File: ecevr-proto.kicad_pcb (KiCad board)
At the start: 4 copper layers, 100 x 92 mm, 218 parts, among them J1 Micro_SD_Card_Det, J1101 USB_microB, J1102 USB_C_Receptacle_USB2.0, J19 SFP, J2 Pwr_fallback, J20 SFP_CAGE, J2001 BNC, J2051 BNC, J2201 BEL_0845_2G1T_H5, J4 JTAG, J5 0821-1X1T-43-F, SW1 SW_Push, SW2101 SW_DIP_x08, U1 TXS0108EPW, U1101 USB3740B-AI9, U1102 UTC2000, U1103 FT231XS, U1104 74LVC1G00, U1105 SC185, U2001 74LVC2T45DC, U2051 74LVC2T45DC, U2101 74LVC1G06, U2102 74LVC1G06, U2103 PCA9306, U2104 24AA0x, U2201 74LVC1G06, U2202 74LVC1G06, U2301 lan9254, U6 PCA9546AD, U8 74AC125, U9 TPS2051B, X2301 FNETHE025

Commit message: WIP: (save)
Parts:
- removed BT1: CR1220, Battery:BatteryHolder_Keystone_500
- removed C1101, C1102, C1103, C1105, C1107: 100nF_603, Capacitor_SMD:C_0603_1608Metric
- removed C1104, C1106, C1108: 22uF_lo_ESR, Capacitor_SMD:C_1812_4532Metric
- removed D1101, D1102, D1103: LED, LED_SMD:LED_0603_1608Metric
- removed FL1101, FL1102, FL3: EMI_Filter_LL_14, proj_footprints:WE_CNSW
- removed H1, H2, H3, H4: MountingHole_Pad, MountingHole:MountingHole_3.2mm_M3_ISO14580_Pad_TopBottom
- removed J1101: USB_microB, Connector_USB:USB_Micro-B_Molex-105017-0001
- removed J1102: USB_C_Receptacle_USB2.0, proj_footprints:USB_C_Receptacle_GCT_USB4085_smaller_holes
- removed J5: 0821-1X1T-43-F, proj_footprints:BEL_0821-1X1T-43-F
- removed JB1: LSHM-150-04_JB1, Connector_Samtec:Samtec_LSHM-150-xx.x-x-DV-S_2x50-1SH_P0.50mm_Vertical
- removed JB2: LSHM-150-04_JB2, Connector_Samtec:Samtec_LSHM-150-xx.x-x-DV-S_2x50-1SH_P0.50mm_Vertical
- removed JB3: LSHM-130-04_JB3, Connector_Samtec:Samtec_LSHM-130-xx.x-x-DV-S_2x30-1SH_P0.50mm_Vertical
- removed JP1101: Jumper_3_Bridged12, Connector_PinHeader_2.54mm:PinHeader_1x03_P2.54mm_Vertical
- removed JP1102: Jumper_NO_Small, Connector_PinHeader_2.54mm:PinHeader_1x02_P2.54mm_Vertical
- removed L1101: 1uH, proj_footprints:L_TDK_SPM6530
- removed R1101, R1104, R1109, R1110: 5k1, Resistor_SMD:R_0603_1608Metric
- removed R1102, R1103, R1116, R1117: 100k, Resistor_SMD:R_0603_1608Metric
- removed R1105, R1106, R1107, R1108, R1111: 10k, Resistor_SMD:R_0603_1608Metric
- removed R1112: 35k7, Resistor_SMD:R_0603_1608Metric
- removed R1113, R1114, R1118: 1k, Resistor_SMD:R_0603_1608Metric
- removed R1115: 1, Resistor_SMD:R_0603_1608Metric
- removed RN1, RN2: 4x4k7, Resistor_SMD:R_Array_Convex_4x0603
- removed U1101: USB3740B-AI9, Package_DFN_QFN:UQFN-10_1.6x2.1mm_P0.5mm
- removed U1102: UTC2000, proj_footprints:QFN-16-1EP_3x3mm_P0.5mm_EP1.8x1.8mm
- removed U1103: FT231XS, Package_SO:SSOP-20_3.9x8.7mm_P0.635mm
- removed U1104: 74LVC1G00, Package_TO_SOT_SMD:SOT-23-5
- removed U1105: SC185, proj_footprints:QFN-16-1EP_3x3mm_P0.5mm_EP1.8x1.8mm
- added C10: 470n, Capacitor_SMD:C_0402_1005Metric, B.Cu at (56.9, 78.0)
- added C11: 100n, Capacitor_SMD:C_0402_1005Metric, B.Cu at (48.7, 72.5)
- added C16: 470n, Capacitor_SMD:C_0402_1005Metric, B.Cu at (56.9, 83.5)
- added C17: 470n, Capacitor_SMD:C_0402_1005Metric, B.Cu at (52.5, 81.7)
- added C18: 4u7, Capacitor_SMD:C_0805_2012Metric, F.Cu at (183.5, 155.2)
- added C19: 470n, Capacitor_SMD:C_0402_1005Metric, B.Cu at (53.9, 79.5)
- added C20: 470n, Capacitor_SMD:C_0402_1005Metric, B.Cu at (53.9, 81.4)
- added C21: 100u, proj_footprints:C_pol_1210_3225Metric, F.Cu at (188.8, 143.7)
- added C22: 470n, Capacitor_SMD:C_0603_1608Metric, F.Cu at (197.7, 146.2)
- added C23: 100n, Capacitor_SMD:C_0402_1005Metric, B.Cu at (45.5, 73.6)
- added C2323: 100n, Capacitor_SMD:C_0603_1608Metric, F.Cu at (172.3, 56.6)
- added C24: 100n, Capacitor_SMD:C_0402_1005Metric, B.Cu at (46.3, 75.2)
- added C25: 4u7, Capacitor_SMD:C_0805_2012Metric, F.Cu at (188.2, 150.3)
- added C26: 47u, Capacitor_SMD:C_1210_3225Metric, F.Cu at (157.8, 195.1)
- added C27: 47u, Capacitor_SMD:C_1210_3225Metric, F.Cu at (165.5, 170.3)
- added C28: 4u7, Capacitor_SMD:C_0805_2012Metric, F.Cu at (161.9, 176.9)
- added C29: 4u7, Capacitor_SMD:C_0805_2012Metric, F.Cu at (169.3, 173.9)
- added C30: 470n, Capacitor_SMD:C_0402_1005Metric, B.Cu at (59.1, 82.1)
- added C31: 470n, Capacitor_SMD:C_0402_1005Metric, B.Cu at (59.1, 85.5)
- added C32: 470n, Capacitor_SMD:C_0402_1005Metric, B.Cu at (52.3, 86.4)
- added C33: 470n, Capacitor_SMD:C_0402_1005Metric, B.Cu at (55.7, 84.9)
- added C34: 47p, Capacitor_SMD:C_0603_1608Metric, F.Cu at (196.3, 161.4)
- added C35: 47p, Capacitor_SMD:C_0603_1608Metric, F.Cu at (191.7, 167.7)
- added C36: 100n, Capacitor_SMD:C_0603_1608Metric, F.Cu at (192.3, 163.9)
- added C37: 10u, Capacitor_SMD:C_1206_3216Metric, F.Cu at (186.9, 168.1)
- added C38: 100n, Capacitor_SMD:C_0603_1608Metric, F.Cu at (196.3, 163.9)
- added C39: 100n, Capacitor_SMD:C_0603_1608Metric, F.Cu at (200.3, 161.4)
- added C40: 470n, Capacitor_SMD:C_0402_1005Metric, B.Cu at (56.2, 75.7)
- added C41: 470n, Capacitor_SMD:C_0402_1005Metric, B.Cu at (59.1, 77.5)
- added C42: 470n, Capacitor_SMD:C_0402_1005Metric, B.Cu at (59.1, 73.5)
- added C43: 470n, Capacitor_SMD:C_0402_1005Metric, B.Cu at (54.3, 75.1)
- added C44: 4u7, Capacitor_SMD:C_0805_2012Metric, F.Cu at (164.9, 173.9)
- added C45: 4u7, Capacitor_SMD:C_0805_2012Metric, F.Cu at (161.9, 179.9)
- added C46: 47u, Capacitor_SMD:C_1210_3225Metric, F.Cu at (171.1, 170.3)
- added C47: 470n, Capacitor_SMD:C_0402_1005Metric, B.Cu at (49.5, 83.1)
- added C48: 470n, Capacitor_SMD:C_0402_1005Metric, B.Cu at (49.5, 84.7)
- added C49: 470n, Capacitor_SMD:C_0402_1005Metric, B.Cu at (46.7, 84.2)
- added C50: 470n, Capacitor_SMD:C_0402_1005Metric, B.Cu at (48.9, 86.2)
- added C51: 4u7, Capacitor_SMD:C_0805_2012Metric, F.Cu at (211.4, 141.4)
- added C52: 4u7, Capacitor_SMD:C_0805_2012Metric, F.Cu at (217.0, 137.2)
- added C53: 47u, Capacitor_SMD:C_1210_3225Metric, F.Cu at (212.0, 137.8)
- added C54: 10u, Capacitor_SMD:C_1206_3216Metric, F.Cu at (25.4, 108.7)
- added C55: 10u, Capacitor_SMD:C_1206_3216Metric, F.Cu at (23.3, 74.5)
- added C6: 4u7, Capacitor_SMD:C_0805_2012Metric, F.Cu at (193.9, 143.0)
- added C62: 10u, Capacitor_SMD:C_1206_3216Metric, F.Cu at (24.3, 86.0)
- added C63: 10u, Capacitor_SMD:C_1206_3216Metric, F.Cu at (25.6, 122.9)
- added C64: 10u, Capacitor_SMD:C_1206_3216Metric, F.Cu at (155.2, 33.2)
- added C65: 22u, Capacitor_SMD:C_1206_3216Metric, F.Cu at (21.5, 100.6)
- added C66: 22u, Capacitor_SMD:C_1206_3216Metric, F.Cu at (26.4, 68.7)
- added C67: 22u, Capacitor_SMD:C_1206_3216Metric, F.Cu at (25.1, 80.3)
- added C68: 10u, Capacitor_SMD:C_1206_3216Metric, F.Cu at (25.2, 115.8)
- added C69: 10u, Capacitor_SMD:C_1206_3216Metric, F.Cu at (155.6, 40.2)
- added C7: 4u7, Capacitor_SMD:C_0805_2012Metric, F.Cu at (174.6, 155.2)
- added C70: 86p, Capacitor_SMD:C_0603_1608Metric, F.Cu at (28.4, 102.3)
- added C71: 86p, Capacitor_SMD:C_0603_1608Metric, F.Cu at (29.8, 69.5)
- added C72: 56p, Capacitor_SMD:C_0603_1608Metric, F.Cu at (28.5, 81.1)
- added C73: 56p, Capacitor_SMD:C_0603_1608Metric, F.Cu at (28.6, 116.6)
- added C74: 130p, Capacitor_SMD:C_0603_1608Metric, F.Cu at (152.2, 39.5)
- added C75: 22u, Capacitor_SMD:C_1206_3216Metric, F.Cu at (25.0, 101.6)
- added C76: 22u, Capacitor_SMD:C_1206_3216Metric, F.Cu at (24.1, 68.7)
- added C77: 100n, Capacitor_SMD:C_0603_1608Metric, F.Cu at (141.3, 160.0)
- added C78: 100n, Capacitor_SMD:C_0603_1608Metric, F.Cu at (163.6, 47.0)
- added C79: 1u, Capacitor_SMD:C_0805_2012Metric, F.Cu at (161.8, 44.4)
- added C8: 4u7, Capacitor_SMD:C_0805_2012Metric, F.Cu at (188.2, 147.3)
- added C80: 100n, Capacitor_SMD:C_0603_1608Metric, F.Cu at (158.4, 45.4)
- added C81: 100n, Capacitor_SMD:C_0603_1608Metric, F.Cu at (156.8, 50.7)
- added C82: 100n, Capacitor_SMD:C_0603_1608Metric, F.Cu at (160.4, 52.8)
- added C83: C_Small, Capacitor_SMD:C_0603_1608Metric, F.Cu at (151.6, 48.5)
- added C84: C_Small, Capacitor_SMD:C_0603_1608Metric, F.Cu at (151.6, 47.0)
- added C85: 100n, Capacitor_SMD:C_0603_1608Metric, F.Cu at (158.9, 52.8)
- added C86: 100n, Capacitor_SMD:C_0603_1608Metric, F.Cu at (156.7, 52.9)
- added C87: 100n, Capacitor_SMD:C_0603_1608Metric, F.Cu at (156.8, 47.7)
- added C88: 1u, Capacitor_SMD:C_0805_2012Metric, F.Cu at (156.4, 54.7)
- added C89: 1u, Capacitor_SMD:C_0805_2012Metric, F.Cu at (154.3, 51.2)
- added C9: 4u7, Capacitor_SMD:C_0805_2012Metric, F.Cu at (170.1, 155.2)
- added C90: 10u, Capacitor_SMD:C_1206_3216Metric, F.Cu at (151.4, 52.5)
- added D9: LED, LED_SMD:LED_0603_1608Metric, F.Cu at (135.0, 150.3)
- added FB1: FB_250, Inductor_SMD:L_0603_1608Metric, F.Cu at (203.5, 136.9)
- added FB2: FB_250, Inductor_SMD:L_0603_1608Metric, F.Cu at (202.1, 144.4)
- added FB3: Ferrite_Bead, Inductor_SMD:L_0603_1608Metric, F.Cu at (163.6, 44.0)
- added J3: USB_C_Receptacle_USB2.0, proj_footprints:USB_C_Receptacle_GCT_USB4085_smaller_holes, F.Cu at (115.3, 137.2)
- added JP2201: 100FDb, Connector_PinHeader_2.54mm:PinHeader_1x03_P2.54mm_Vertical, F.Cu at (144.5, 33.0)
- added L1: 2u2, Inductor_SMD:L_Taiyo-Yuden_NR-50xx, F.Cu at (21.1, 104.7)
- added L4: 1u, Inductor_SMD:L_Taiyo-Yuden_NR-50xx, F.Cu at (20.1, 70.5)
- added L5: 1u, Inductor_SMD:L_Taiyo-Yuden_NR-50xx, F.Cu at (21.1, 82.0)
- added L6: 2u2, Inductor_SMD:L_Taiyo-Yuden_NR-50xx, F.Cu at (21.4, 118.9)
- added L7: 2u2, Inductor_SMD:L_Taiyo-Yuden_NR-50xx, F.Cu at (159.4, 37.1)
- added R14: 1k, Resistor_SMD:R_0603_1608Metric, F.Cu at (68.4, 71.7)
- added R15: 2k4, Resistor_SMD:R_0603_1608Metric, F.Cu at (166.1, 176.7)
- added R16: 2k4, Resistor_SMD:R_0603_1608Metric, F.Cu at (166.1, 179.2)
- added R17: 2k4, Resistor_SMD:R_0603_1608Metric, F.Cu at (173.5, 173.7)
- added R18: 50, Resistor_SMD:R_0603_1608Metric, F.Cu at (66.9, 76.8)
- added R19: 0, Resistor_SMD:R_0402_1005Metric, F.Cu at (199.8, 163.7)
- added R20: 27, Resistor_SMD:R_0603_1608Metric, F.Cu at (192.3, 161.4)
- added R21: 27, Resistor_SMD:R_0603_1608Metric, F.Cu at (195.7, 166.4)
- added R2114: 100k, Resistor_SMD:R_0603_1608Metric, F.Cu at (169.1, 103.6)
- added R22: 10k, Resistor_SMD:R_0603_1608Metric, F.Cu at (28.4, 108.3)
- added R2211: 100, Resistor_SMD:R_0603_1608Metric, F.Cu at (166.0, 41.2)
- added R23: 10k, Resistor_SMD:R_0603_1608Metric, F.Cu at (19.5, 74.9)
- added R2304: 50, Resistor_SMD:R_0603_1608Metric, F.Cu at (170.1, 56.7)
- added R24: 10k, Resistor_SMD:R_0603_1608Metric, F.Cu at (20.5, 86.4)
- added R25: 10k, Resistor_SMD:R_0603_1608Metric, F.Cu at (28.6, 122.5)
- added R33: 10k, Resistor_SMD:R_0603_1608Metric, F.Cu at (152.1, 33.5)
- added R35: 10k, Resistor_SMD:R_0603_1608Metric, F.Cu at (141.3, 162.5)
- added R36: 24k, Resistor_SMD:R_0603_1608Metric, F.Cu at (28.4, 105.3)
- added R37: 24k, Resistor_SMD:R_0603_1608Metric, F.Cu at (26.4, 72.5)
- added R38: 24k, Resistor_SMD:R_0603_1608Metric, F.Cu at (27.4, 84.1)
- added R39: 12k, Resistor_SMD:R_0603_1608Metric, F.Cu at (28.6, 119.5)
- added R40: 45.9k, Resistor_SMD:R_0603_1608Metric, F.Cu at (152.1, 36.5)
- added R41: 16k, Resistor_SMD:R_0603_1608Metric, F.Cu at (26.9, 102.3)
- added R42: 16k, Resistor_SMD:R_0603_1608Metric, F.Cu at (28.3, 69.5)
- added R43: 24k, Resistor_SMD:R_0603_1608Metric, F.Cu at (27.0, 81.1)
- added R44: 24k, Resistor_SMD:R_0603_1608Metric, F.Cu at (27.1, 116.5)
- added R45: 10.2k, Resistor_SMD:R_0603_1608Metric, F.Cu at (153.7, 39.5)
- added R46: 0, Resistor_SMD:R_0603_1608Metric, F.Cu at (27.6, 100.0)
- added R47: 0, Resistor_SMD:R_0603_1608Metric, F.Cu at (29.1, 67.2)
- added R48: 0, Resistor_SMD:R_0603_1608Metric, F.Cu at (27.8, 78.8)
- added R49: 0, Resistor_SMD:R_0603_1608Metric, F.Cu at (27.9, 114.2)
- added R50: 0, Resistor_SMD:R_0603_1608Metric, F.Cu at (152.9, 41.8)
- added R51: 1k, Resistor_SMD:R_0603_1608Metric, F.Cu at (155.2, 142.2)
- added R52: 100k, Resistor_SMD:R_0603_1608Metric, F.Cu at (151.2, 142.2)
- added R53: 100k, Resistor_SMD:R_0603_1608Metric, F.Cu at (156.5, 149.7)
- added R54: 10k, Resistor_SMD:R_0603_1608Metric, F.Cu at (154.9, 157.2)
- added R55: 10k, Resistor_SMD:R_0603_1608Metric, F.Cu at (145.3, 160.3)
- added R56: 5k1, Resistor_SMD:R_0603_1608Metric, F.Cu at (160.5, 149.4)
- added R57: 5k1, Resistor_SMD:R_0603_1608Metric, F.Cu at (154.9, 154.7)
- added R58: 10k, Resistor_SMD:R_0603_1608Metric, F.Cu at (149.3, 160.3)
- added R59: 10k, Resistor_SMD:R_0603_1608Metric, F.Cu at (150.9, 157.2)
- added R60: 5k1, Resistor_SMD:R_0603_1608Metric, F.Cu at (145.3, 162.8)
- added R61: 35k7, Resistor_SMD:R_0603_1608Metric, F.Cu at (151.1, 144.7)
- added R62: 0.01, Resistor_SMD:R_1206_3216Metric, F.Cu at (141.4, 147.3)
- added R63: 4k7, Resistor_SMD:R_0603_1608Metric, F.Cu at (67.0, 61.1)
- added R64: 10k, Resistor_SMD:R_0603_1608Metric, F.Cu at (156.2, 44.4)
- added R65: 10k, Resistor_SMD:R_0603_1608Metric, F.Cu at (159.3, 43.8)
- added R66: 1k78, Resistor_SMD:R_0603_1608Metric, F.Cu at (164.3, 53.6)
- added R67: 50, Resistor_SMD:R_0603_1608Metric, F.Cu at (154.6, 48.5)
- added R68: 50, Resistor_SMD:R_0603_1608Metric, F.Cu at (154.6, 47.0)
- added R69: 33, Resistor_SMD:R_0603_1608Metric, F.Cu at (162.1, 52.8)
- added R70: 0, Resistor_SMD:R_0603_1608Metric, F.Cu at (154.3, 44.1)
- added R71: 0, Resistor_SMD:R_0603_1608Metric, F.Cu at (154.0, 53.7)
- added TP1: TestPoint_Small, TestPoint:TestPoint_Pad_D1.0mm, F.Cu at (129.3, 169.7)
- added TP10: TestPoint_Small, TestPoint:TestPoint_Pad_D1.0mm, F.Cu at (114.0, 188.0)
- added TP11: TestPoint_Small, TestPoint:TestPoint_Pad_D1.0mm, F.Cu at (141.5, 178.8)
- added TP12: TestPoint_Small, TestPoint:TestPoint_Pad_D1.0mm, F.Cu at (129.3, 175.8)
- added TP13: TestPoint_Small, TestPoint:TestPoint_Pad_D1.0mm, F.Cu at (126.2, 178.8)
- added TP14: TestPoint_Small, TestPoint:TestPoint_Pad_D1.0mm, F.Cu at (126.2, 184.9)
- added TP15: TestPoint_Small, TestPoint:TestPoint_Pad_D1.0mm, F.Cu at (144.5, 175.8)
- added TP16: TestPoint_Small, TestPoint:TestPoint_Pad_D1.0mm, F.Cu at (147.6, 172.7)
- added TP17: TestPoint_Small, TestPoint:TestPoint_Pad_D1.0mm, F.Cu at (138.4, 178.8)
- added TP18: TestPoint_Small, TestPoint:TestPoint_Pad_D1.0mm, F.Cu at (138.4, 184.9)
- added TP19: TestPoint_Small, TestPoint:TestPoint_Pad_D1.0mm, F.Cu at (141.5, 181.9)
- added TP2: TestPoint_Small, TestPoint:TestPoint_Pad_D1.0mm, F.Cu at (120.1, 184.9)
- added TP20: TestPoint_Small, TestPoint:TestPoint_Pad_D1.0mm, F.Cu at (144.5, 178.8)
- added TP21: TestPoint_Small, TestPoint:TestPoint_Pad_D1.0mm, F.Cu at (147.6, 175.8)
- added TP22: TestPoint_Small, TestPoint:TestPoint_Pad_D1.0mm, F.Cu at (138.4, 188.0)
- added TP23: TestPoint_Small, TestPoint:TestPoint_Pad_D1.0mm, F.Cu at (141.5, 184.9)
- added TP24: TestPoint_Small, TestPoint:TestPoint_Pad_D1.0mm, F.Cu at (144.5, 181.9)
- added TP25: TestPoint_Small, TestPoint:TestPoint_Pad_D1.0mm, F.Cu at (147.6, 178.8)
- added TP26: TestPoint_Small, TestPoint:TestPoint_Pad_D1.0mm, F.Cu at (126.2, 188.0)
- added TP27: TestPoint_Small, TestPoint:TestPoint_Pad_D1.0mm, F.Cu at (135.4, 172.7)
- added TP28: TestPoint_Small, TestPoint:TestPoint_Pad_D1.0mm, F.Cu at (138.4, 169.7)
- added TP29: TestPoint_Small, TestPoint:TestPoint_Pad_D1.0mm, F.Cu at (123.2, 188.0)
- added TP3: TestPoint_Small, TestPoint:TestPoint_Pad_D1.0mm, F.Cu at (117.1, 188.0)
- added TP30: TestPoint_Small, TestPoint:TestPoint_Pad_D1.0mm, F.Cu at (135.4, 181.9)
- added TP31: TestPoint_Small, TestPoint:TestPoint_Pad_D1.0mm, F.Cu at (132.3, 184.9)
- added TP32: TestPoint_Small, TestPoint:TestPoint_Pad_D1.0mm, F.Cu at (129.3, 188.0)
- added TP33: TestPoint_Small, TestPoint:TestPoint_Pad_D1.0mm, F.Cu at (144.5, 169.7)
- added TP34: TestPoint_Small, TestPoint:TestPoint_Pad_D1.0mm, F.Cu at (141.5, 172.7)
- added TP35: TestPoint_Small, TestPoint:TestPoint_Pad_D1.0mm, F.Cu at (138.4, 175.8)
- added TP36: TestPoint_Small, TestPoint:TestPoint_Pad_D1.0mm, F.Cu at (135.4, 178.8)
- added TP37: TestPoint_Small, TestPoint:TestPoint_Pad_D1.0mm, F.Cu at (132.3, 181.9)
- added TP38: TestPoint_Small, TestPoint:TestPoint_Pad_D1.0mm, F.Cu at (129.3, 184.9)
- added TP39: TestPoint_Small, TestPoint:TestPoint_Pad_D1.0mm, F.Cu at (132.3, 175.8)
- added TP4: TestPoint_Small, TestPoint:TestPoint_Pad_D1.0mm, F.Cu at (132.3, 169.7)
- added TP40: TestPoint_Small, TestPoint:TestPoint_Pad_D1.0mm, F.Cu at (135.4, 188.0)
- added TP41: TestPoint_Small, TestPoint:TestPoint_Pad_D1.0mm, F.Cu at (141.5, 169.7)
- added TP42: TestPoint_Small, TestPoint:TestPoint_Pad_D1.0mm, F.Cu at (135.4, 175.8)
- added TP43: TestPoint_Small, TestPoint:TestPoint_Pad_D1.0mm, F.Cu at (132.3, 178.8)
- added TP44: TestPoint_Small, TestPoint:TestPoint_Pad_D1.0mm, F.Cu at (129.3, 181.9)
- added TP45: TestPoint_Small, TestPoint:TestPoint_Pad_D1.0mm, F.Cu at (138.4, 172.7)
- added TP46: TestPoint_Small, TestPoint:TestPoint_Pad_D1.0mm, F.Cu at (123.2, 169.7)
- added TP47: TestPoint_Small, TestPoint:TestPoint_Pad_D1.0mm, F.Cu at (132.3, 172.7)
- added TP48: TestPoint_Small, TestPoint:TestPoint_Pad_D1.0mm, F.Cu at (135.4, 169.7)
- added TP49: TestPoint_Small, TestPoint:TestPoint_Pad_D1.0mm, F.Cu at (120.1, 188.0)
- added TP5: TestPoint_Small, TestPoint:TestPoint_Pad_D1.0mm, F.Cu at (129.3, 172.7)
- added TP50: TestPoint_Small, TestPoint:TestPoint_Pad_D1.0mm, F.Cu at (123.2, 184.9)
- added TP51: TestPoint_Small, TestPoint:TestPoint_Pad_D1.0mm, F.Cu at (126.2, 181.9)
- added TP52: TestPoint_Small, TestPoint:TestPoint_Pad_D1.0mm, F.Cu at (129.3, 178.8)
- added TP53: TestPoint_Small, TestPoint:TestPoint_Pad_D1.0mm, F.Cu at (114.0, 181.9)
- added TP54: TestPoint_Small, TestPoint:TestPoint_Pad_D1.0mm, F.Cu at (114.0, 172.7)
- added TP55: TestPoint_Small, TestPoint:TestPoint_Pad_D1.0mm, F.Cu at (117.1, 169.7)
- added TP56: TestPoint_Small, TestPoint:TestPoint_Pad_D1.0mm, F.Cu at (114.0, 175.8)
- added TP57: TestPoint_Small, TestPoint:TestPoint_Pad_D1.0mm, F.Cu at (117.1, 172.7)
- added TP58: TestPoint_Small, TestPoint:TestPoint_Pad_D1.0mm, F.Cu at (120.1, 169.7)
- added TP59: TestPoint_Small, TestPoint:TestPoint_Pad_D1.0mm, F.Cu at (114.0, 178.8)
- added TP6: TestPoint_Small, TestPoint:TestPoint_Pad_D1.0mm, F.Cu at (126.2, 175.8)
- added TP60: TestPoint_Small, TestPoint:TestPoint_Pad_D1.0mm, F.Cu at (117.1, 175.8)
- added TP61: TestPoint_Small, TestPoint:TestPoint_Pad_D1.0mm, F.Cu at (120.1, 172.7)
- added TP62: TestPoint_Small, TestPoint:TestPoint_Pad_D1.0mm, F.Cu at (120.1, 178.8)
- added TP63: TestPoint_Small, TestPoint:TestPoint_Pad_D1.0mm, F.Cu at (135.4, 184.9)
- added TP64: TestPoint_Small, TestPoint:TestPoint_Pad_D1.0mm, F.Cu at (132.3, 188.0)
- added TP65: TestPoint_Small, TestPoint:TestPoint_Pad_D1.0mm, F.Cu at (147.6, 169.7)
- added TP66: TestPoint_Small, TestPoint:TestPoint_Pad_D1.0mm, F.Cu at (144.5, 172.7)
- added TP67: TestPoint_Small, TestPoint:TestPoint_Pad_D1.0mm, F.Cu at (141.5, 175.8)
- added TP68: TestPoint_Small, TestPoint:TestPoint_Pad_D1.0mm, F.Cu at (123.2, 181.9)
- added TP69: TestPoint_Small, TestPoint:TestPoint_Pad_D1.0mm, F.Cu at (126.2, 172.7)
- added TP7: TestPoint_Small, TestPoint:TestPoint_Pad_D1.0mm, F.Cu at (123.2, 178.8)
- added TP70: TestPoint_Small, TestPoint:TestPoint_Pad_D1.0mm, F.Cu at (123.2, 175.8)
- added TP71: TestPoint_Small, TestPoint:TestPoint_Pad_D1.0mm, F.Cu at (138.4, 181.9)
- added TP72: TestPoint_Small, TestPoint:TestPoint_Pad_D1.0mm, F.Cu at (117.1, 181.9)
- added TP73: TestPoint_Small, TestPoint:TestPoint_Pad_D1.0mm, F.Cu at (114.0, 184.9)
- added TP74: TestPoint_Small, TestPoint:TestPoint_Pad_D1.0mm, F.Cu at (126.2, 169.7)
- added TP75: TestPoint_Small, TestPoint:TestPoint_Pad_D1.0mm, F.Cu at (123.2, 172.7)
- added TP76: TestPoint_Small, TestPoint:TestPoint_Pad_D1.0mm, F.Cu at (120.1, 175.8)
- added TP77: TestPoint_Small, TestPoint:TestPoint_Pad_D1.0mm, F.Cu at (117.1, 178.8)
- added TP78: TestPoint_Small, TestPoint:TestPoint_Pad_D1.0mm, F.Cu at (114.0, 169.7)
- added TP8: TestPoint_Small, TestPoint:TestPoint_Pad_D1.0mm, F.Cu at (120.1, 181.9)
- added TP9: TestPoint_Small, TestPoint:TestPoint_Pad_D1.0mm, F.Cu at (117.1, 184.9)
- added U10: 74LVC1G02, Package_TO_SOT_SMD:SOT-23-5, F.Cu at (146.7, 144.7)
- added U11: UTC2000, Package_DFN_QFN:QFN-16-1EP_3x3mm_P0.5mm_EP1.75x1.75mm_ThermalVias, F.Cu at (151.9, 138.3)
- added U12: 5P49V6965, Package_DFN_QFN:QFN-24-1EP_4x4mm_P0.5mm_EP2.8x2.8mm, F.Cu at (160.2, 48.7)
- added U2: AT25SL641, Package_SON:WSON-8-1EP_6x5mm_P1.27mm_EP3.4x4mm, F.Cu at (56.8, 67.0)
- added U2105: 74AHC1T86, Package_TO_SOT_SMD:SOT-353_SC-70-5, F.Cu at (166.8, 106.8)
- added U2106: 74AHC1T86, Package_TO_SOT_SMD:SOT-353_SC-70-5, F.Cu at (194.5, 86.7)
- added U2302: SN74LV1T34DBV, Package_TO_SOT_SMD:SOT-23-5, F.Cu at (175.0, 57.6)
- added U3: FT240XQ, Package_DFN_QFN:QFN-24-1EP_4x4mm_P0.5mm_EP2.6x2.6mm, F.Cu at (187.2, 163.3)
- added U4: TLV62569ADDC, Package_TO_SOT_SMD:SOT-23-6, F.Cu at (25.8, 105.7)
- added U5: TPS62A01A-SOT563, Package_TO_SOT_SMD:SOT-563, F.Cu at (24.2, 72.2)
- added U7: TLV62569ADDC, Package_TO_SOT_SMD:SOT-23-6, F.Cu at (26.0, 119.9)
- added Y1: 25MHz, Crystal:Crystal_SMD_Abracon_ABM10-4Pin_2.5x2.0mm, F.Cu at (164.3, 50.2)
- C12, C13, C2: value 100nF_603 -> 470n; footprint Capacitor_SMD:C_0603_1608Metric -> Capacitor_SMD:C_0402_1005Metric; moved to B.Cu
- C14: value 47uF, 10V -> 470n; footprint Capacitor_SMD:C_1206_3216Metric -> Capacitor_SMD:C_0402_1005Metric; moved to B.Cu
- C15: value 47uF, 10V -> 100n; footprint Capacitor_SMD:C_1206_3216Metric -> Capacitor_SMD:C_0402_1005Metric; moved to B.Cu
- C3: value 100nF_603 -> 330u; footprint Capacitor_SMD:C_0603_1608Metric -> Capacitor_Tantalum_SMD:CP_EIA-7343-30_AVX-N
- C4: value 10u -> 47u; footprint Capacitor_SMD:C_1206_3216Metric -> Capacitor_SMD:C_1210_3225Metric
- C5: value 100nF_603 -> 4u7; footprint Capacitor_SMD:C_0603_1608Metric -> Capacitor_SMD:C_0805_2012Metric
- J1: value Micro_SD_Card_Det -> PEN_SEL; footprint proj_footprints:microSD_HC_Hirose_DM3D-SF_smaller_crtyd -> Connector_PinHeader_2.54mm:PinHeader_2x03_P2.54mm_Vertical
- J2: value Pwr_fallback -> PEN_SEL; footprint Connector_PinSocket_2.54mm:PinSocket_2x06_P2.54mm_Vertical -> Connector_PinHeader_2.54mm:PinHeader_2x03_P2.54mm_Vertical
- JP1: value TEST -> JTAG_boot
- JP2: value Jumper -> INITb
- JP3: value Jumper_NO_Small -> PUDC_dis
- R1: value 10k -> 100
- R11: value 100 -> 1k
- R12: value 100 -> 4k7
- R13: value 10k -> 4k7
- R2: value 10k -> 50
- R2107: value 1k -> 100k
- R34: value 10k -> 0
- SW1: value SW_Push -> PROG
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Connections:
- C1 pad 1: OTG_ID -> GND
- C1 pad 2: +3V3 -> +1V8
- C12 pad 1: +5V -> +1V0
- C12 pad 2: OTG_ID -> GND
- C13 pad 1: Net-(C13-Pad1) -> +1V8
- C13 pad 2: OTG_ID -> GND
- C14 pad 1: Net-(C14-Pad1) -> +1V0
- C14 pad 2: OTG_ID -> GND
- C15 pad 1: Net-(C14-Pad1) -> /fpga/1V0_MGT
- C15 pad 2: OTG_ID -> GND
- C2 pad 1: +3V3 -> Net-(C2-Pad1)
- C2 pad 2: OTG_ID -> /fpga/fpga_bank0_cfg/AGND
- C2001 pad 2: OTG_ID -> GND
- C2002 pad 2: OTG_ID -> GND
- C2051 pad 2: OTG_ID -> GND
- C2052 pad 2: OTG_ID -> GND
- C2101 pad 2: OTG_ID -> GND
- C2102 pad 2: OTG_ID -> GND
- C2103 pad 1: +3V3 -> +1V8
- C2103 pad 2: OTG_ID -> GND
- C2201 pad 2: OTG_ID -> GND
- C2202 pad 2: OTG_ID -> GND
- C2203 pad 2: OTG_ID -> GND
- C2204 pad 2: OTG_ID -> GND
- C2205 pad 2: OTG_ID -> GND
- C2206 pad 2: OTG_ID -> GND
- C2207 pad 2: OTG_ID -> GND
- C2208 pad 2: OTG_ID -> GND
- C2209 pad 2: OTG_ID -> GND
- C2210 pad 2: OTG_ID -> GND
- C2301 pad 2: OTG_ID -> GND
- C2302 pad 2: OTG_ID -> GND
- C2303 pad 2: OTG_ID -> GND
- C2304 pad 2: OTG_ID -> GND
- C2305 pad 2: OTG_ID -> GND
- C2306 pad 2: OTG_ID -> GND
- C2307 pad 2: OTG_ID -> GND
- C2308 pad 1: OTG_ID -> GND
- C2309 pad 1: OTG_ID -> GND
- C2310 pad 1: OTG_ID -> GND
- C2311 pad 2: OTG_ID -> GND
- C2312 pad 1: OTG_ID -> GND
- C2313 pad 2: OTG_ID -> GND
- C2314 pad 1: OTG_ID -> GND
- C2315 pad 2: OTG_ID -> GND
- C2316 pad 2: OTG_ID -> GND
- C2317 pad 2: OTG_ID -> GND
- C2318 pad 2: OTG_ID -> GND
- C2319 pad 2: OTG_ID -> GND
- C2320 pad 2: OTG_ID -> GND
- C2321 pad 2: OTG_ID -> GND
- C2322 pad 2: OTG_ID -> GND
- C3 pad 1: +3V3 -> +1V0
- C3 pad 2: OTG_ID -> GND
- C4 pad 1: OTG_ID -> +1V8
- C4 pad 2: +3V3 -> GND
- C5 pad 2: OTG_ID -> GND
- C56 pad 2: OTG_ID -> GND
- C57 pad 2: OTG_ID -> GND
- C58 pad 2: OTG_ID -> GND
- C59 pad 2: OTG_ID -> GND
- C60 pad 2: OTG_ID -> GND
- C61 pad 2: OTG_ID -> GND
- D1 pad 1: OTG_ID -> GND
- D2 pad 1: OTG_ID -> GND
- D2101 pad 1: Net-(D2101-Pad1) -> GND
- D2101 pad 2: +3V3 -> Net-(D2101-Pad2)
- D2102 pad 1: Net-(D2102-Pad1) -> GND
- D2102 pad 2: +3V3 -> Net-(D2102-Pad2)
- D3 pad 1: OTG_ID -> GND
- D4 pad 1: OTG_ID -> GND
- D5 pad 1: OTG_ID -> GND
- D6 pad 1: OTG_ID -> GND
- D7 pad 1: OTG_ID -> GND
- D8 pad 1: OTG_ID -> GND
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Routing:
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- added copper zone on In2.Cu, net +1V0
- added copper zone on In2.Cu, net +1V8
- added copper zone on In2.Cu, net /fpga/1V0_MGT
- added copper zone on In2.Cu, net /fpga/1V2_MGT
- added copper zone on B.Cu, net GND
- added copper zone on In1.Cu, net GND
- removed copper zone on F.Cu, net +3V3
- removed copper zone on F.Cu, net +3V3_PWR_OUT
- removed copper zone on B.Cu, net +5V
- removed copper zone on F.Cu, net +5V
- removed copper zone on F.Cu, net Net-(L1101-Pad2)
- removed copper zone on B.Cu, net OTG_ID
- removed copper zone on F.Cu, net OTG_ID
- removed copper zone on In1.Cu, net OTG_ID
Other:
- net class Default: clearance 0.1524 -> 0.0889
- rule trace_clearance: 0.1524 -> 0.0889

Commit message: WIP: point before we change to OSH/relaxed process
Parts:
- removed TP1, TP10, TP11, TP12, TP13, TP14, TP15, TP16, TP17, TP18, TP19, TP2, TP20, TP21, TP22, TP23, TP24, TP25, TP26, TP27, TP28, TP29, TP3, TP30, TP31, TP32, TP33, TP34, TP35, TP36, TP37, TP38, TP39, TP4, TP40, TP41, TP42, TP43, TP44, TP45, TP46, TP47, TP48, TP49, TP5, TP50, TP51, TP52, TP53, TP54, TP55, TP56, TP57, TP58, TP59, TP6, TP60, TP61, TP62, TP63, TP64, TP65, TP66, TP67, TP68, TP69, TP7, TP70, TP71, TP72, TP73, TP74, TP75, TP76, TP77, TP78, TP8, TP9: TestPoint_Small, TestPoint:TestPoint_Pad_D1.0mm
- added C100: 100nF, Capacitor_SMD:C_0603_1608Metric, F.Cu at (33.9, 183.1)
- added C101: 1uF, Capacitor_SMD:C_0805_2012Metric, F.Cu at (-10.0, 198.8)
- added C102: 1uF, Capacitor_SMD:C_0805_2012Metric, F.Cu at (-5.58, 198.8)
- added C103: 100nF, Capacitor_SMD:C_0603_1608Metric, F.Cu at (34.3, 175.6)
- added C104: 100nF, Capacitor_SMD:C_0603_1608Metric, F.Cu at (34.3, 178.1)
- added C91: 100n, Capacitor_SMD:C_0603_1608Metric, F.Cu at (60.2, 174.5)
- added C92: 100n, Capacitor_SMD:C_0603_1608Metric, F.Cu at (45.8, 180.1)
- added C93: 220u, Capacitor_Tantalum_SMD:CP_EIA-6032-28_Kemet-C, F.Cu at (48.1, 173.1)
- added C94: 1n, Capacitor_SMD:C_0603_1608Metric, F.Cu at (53.8, 181.5)
- added C95: 100nF, Capacitor_SMD:C_0603_1608Metric, F.Cu at (29.9, 181.5)
- added C96: 100nF, Capacitor_SMD:C_0603_1608Metric, F.Cu at (7.50, 198.6)
- added C97: 1uF, Capacitor_SMD:C_0805_2012Metric, F.Cu at (-1.14, 198.8)
- added C98: 1uF, Capacitor_SMD:C_0805_2012Metric, F.Cu at (30.1, 175.8)
- added C99: 100nF, Capacitor_SMD:C_0603_1608Metric, F.Cu at (11.5, 198.6)
- added D10: HFBR2528, proj_footprints:HFBR25XX, F.Cu at (-8.66, 178.4)
- added D11: HFBR1528, proj_footprints:HFBR25XX, F.Cu at (-8.66, 191.6)
- added D12: HFBR2528, proj_footprints:HFBR25XX, F.Cu at (11.4, 178.4)
- added D13: HFBR1528, proj_footprints:HFBR25XX, F.Cu at (11.4, 191.6)
- added Q1: SSM6N35AFE, proj_footprints:SOT-563-adjusted, F.Cu at (163.2, 39.1)
- added Q2: SSM6N35AFE, proj_footprints:SOT-563-adjusted, F.Cu at (59.7, 177.2)
- added Q3: Si3477, Package_TO_SOT_SMD:TSOT-23-6, F.Cu at (55.0, 173.0)
- added R2115: 10k, Resistor_SMD:R_0603_1608Metric, F.Cu at (-10.3, 204.8)
- added R72: 3k3, Resistor_SMD:R_0603_1608Metric, F.Cu at (83.7, 152.2)
- added R73: 10k, Resistor_SMD:R_0603_1608Metric, F.Cu at (140.3, 32.2)
- added R74: 10k, Resistor_SMD:R_0603_1608Metric, F.Cu at (141.8, 32.2)
- added R75: 100k, Resistor_SMD:R_0603_1608Metric, F.Cu at (56.2, 179.0)
- added R76: 100k, Resistor_SMD:R_0603_1608Metric, F.Cu at (56.2, 176.5)
- added R77: 47, Resistor_SMD:R_1206_3216Metric, F.Cu at (46.6, 177.2)
- added R78: 100k, Resistor_SMD:R_0603_1608Metric, F.Cu at (49.8, 181.4)
- added R79: 10k, Resistor_SMD:R_0603_1608Metric, F.Cu at (59.7, 172.0)
- added R80: 100k, Resistor_SMD:R_0603_1608Metric, F.Cu at (38.3, 175.6)
- added R81: 100k, Resistor_SMD:R_0603_1608Metric, F.Cu at (34.3, 180.6)
- added R82: 1k, Resistor_SMD:R_0603_1608Metric, F.Cu at (29.9, 184.0)
- added R83: 1k, Resistor_SMD:R_0603_1608Metric, F.Cu at (15.5, 198.6)
- added R84: 1k, Resistor_SMD:R_0603_1608Metric, F.Cu at (38.3, 178.1)
- added R85: 1k, Resistor_SMD:R_0603_1608Metric, F.Cu at (29.9, 186.5)
- added R86: 90, Resistor_SMD:R_0805_2012Metric, F.Cu at (30.1, 178.8)
- added R87: 90, Resistor_SMD:R_0805_2012Metric, F.Cu at (3.29, 198.8)
- added U13: TPS3808DBV, Package_TO_SOT_SMD:SOT-23-6, F.Cu at (51.8, 177.8)
- added U14: 74LVC1G06, proj_footprints:SOT-5x3, F.Cu at (150.2, 35.5)
- added U15: 74LVC2T45DC, Package_SO:VSSOP-8_2.3x2mm_P0.5mm, F.Cu at (30.7, 172.5)
- added U16: 74LVC2T45DC, Package_SO:VSSOP-8_2.3x2mm_P0.5mm, F.Cu at (36.2, 172.5)
- C83, C84: value C_Small -> 100n
- J1: value PEN_SEL -> CUR_SEL
- R2: value 50 -> 3k3
- R64, R65: value 10k -> 3k3
- U10: value 74LVC1G02 -> 74VHC1G03
- moved C39 175.7 mm to (43.0, 83.2)
- moved R19 171.5 mm to (45.4, 89.0)
- moved FB2 168.2 mm to (52.0, 68.5), turned to 270 degrees
- moved FB1 167.5 mm to (52.0, 65.5), turned to 90 degrees
- moved U3 164.3 mm to (41.9, 86.6), turned to 270 degrees
- moved R15 160.4 mm to (50.5, 65.5), turned to 90 degrees
- moved R16 156.1 mm to (60.2, 64.4), turned to 270 degrees
- moved R17 155.4 mm to (61.7, 65.8), turned to 270 degrees
- moved C86 104.4 mm to (53.6, 69.9), turned to 270 degrees
- moved J3 100.8 mm to (30.6, 82.7), turned to 270 degrees
- moved R2 90.2 mm to (76.8, 156.9), turned to 0 degrees
- moved H7 47.9 mm to (104.2, 117.9)
- moved C1 46.0 mm to (54.9, 104.8)
- moved J4 46.0 mm to (42.1, 105.8)
- moved R26 46.0 mm to (58.9, 104.8)
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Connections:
- net /USB, SDIO, RJ45, JTAG, UART, I2C/USBD_N renamed /USB, JTAG, I2C/USBD_N
- net /USB, SDIO, RJ45, JTAG, UART, I2C/USBD_P renamed /USB, JTAG, I2C/USBD_P
- C86 pad 1: GND -> +1V8
- C86 pad 2: +1V8 -> GND
- J19 pad 2: B13_L6_P -> IO_L7N_T1_AD2N_15
- J19 pad 3: B13_L6_N -> /SFP Connector/TX_DISABLE
- J19 pad 4: SDA1 -> SDA1_3V3
- J19 pad 5: SCL1 -> SCL1_3V3
- J19 pad 6: B13_L4_P -> IO_L5N_T0_AD9N_15
- J19 pad 8: B13_L4_N -> IO_L4N_T0_15
- J2 pad 4: USB_PWRENb -> IO_L15N_T2_DQS_34
- R10 pad 1: B13_L18_P -> IO_L20P_T3_34
- R19 pad 1: FIFO_CLK -> IO_L12P_T1_MRCC_34
- R2 pad 1: /fpga/fpga_bank0_cfg/CCLK -> +1V8
- R2 pad 2: Net-(R2-Pad2) -> IO_L23N_T3_A02_D18_14
- R2001 pad 2: B35_L10_P -> IO_L18N_T2_A11_D27_14
- R2002 pad 1: B35_L20_N -> IO_L13N_T2_MRCC_14
- R2003 pad 1: B35_L10_P -> IO_L18N_T2_A11_D27_14
- R2051 pad 2: B35_L20_P -> IO_L18P_T2_A12_D28_14
- R2052 pad 1: B35_L25 -> IO_L17N_T2_A13_D29_14
- R2053 pad 1: B35_L20_P -> IO_L18P_T2_A12_D28_14
- R2106 pad 1: B35_L3_N -> IO_L3N_T0_DQS_EMCCLK_14
- R2112 pad 1: Net-(R2112-Pad1) -> IO_L21P_T3_DQS_14
- R2113 pad 2: Net-(R2112-Pad1) -> IO_L21P_T3_DQS_14
- R2114 pad 2: Net-(R2114-Pad2) -> IO_L22P_T3_A05_D21_14
- R3 pad 1: B13_L15_N -> IO_L3P_T0_DQS_34
- R4 pad 1: B13_L15_P -> IO_L3N_T0_DQS_34
- R5 pad 1: B13_L20_P -> IO_L18N_T2_34
- R53 pad 1: Net-(J1-Pad1) -> +5V
- R53 pad 2: +5V -> Net-(J1-Pad1)
- R6 pad 1: B13_L20_N -> IO_L18P_T2_34
- R62 pad 2: VBUS -> Net-(Q3-Pad1)
- R64 pad 1: I2C_SCL -> IO_L7P_T1_AD2P_15
- R65 pad 1: I2C_SDA -> IO_L8P_T1_AD10P_15
- R7 pad 1: B13_L21_P -> IO_25_34
- R8 pad 1: B13_L21_N -> IO_L20N_T3_34
- R9 pad 1: B13_L18_N -> IO_L23N_T3_34
- SW2101 pad 10: Net-(SW2101-Pad10) -> IO_L21N_T3_DQS_A06_D22_14
- SW2101 pad 12: Net-(R2114-Pad2) -> IO_L22P_T3_A05_D21_14
- SW2101 pad 15: Net-(R2112-Pad1) -> IO_L21P_T3_DQS_14
- SW2101 pad 7: Net-(SW2101-Pad7) -> GND
- SW2101 pad 8: Net-(SW2101-Pad8) -> GND
- SW2101 pad 9: Net-(SW2101-Pad9) -> IO_L22N_T3_A04_D20_14
- U1 pad E8: Net-(R2-Pad2) -> /fpga/fpga_bank0_cfg/CCLK
- U12 pad 8: I2C_SDA -> IO_L8P_T1_AD10P_15
- U12 pad 9: I2C_SCL -> IO_L7P_T1_AD2P_15
- U2001 pad 5: B35_L20_N -> IO_L13N_T2_MRCC_14
- U2051 pad 5: B35_L25 -> IO_L17N_T2_A13_D29_14
- U2103 pad 5: SDA0 -> IO_L23N_T3_A02_D18_14
- U2103 pad 6: SCL0 -> IO_L23P_T3_A03_D19_14
- U2104 pad 1: SCL0 -> IO_L23P_T3_A03_D19_14
- U2104 pad 3: SDA0 -> IO_L23N_T3_A02_D18_14
- U2104 pad 5: GND -> IO_25_14
- U2105 pad 1: Net-(R2114-Pad2) -> IO_L22P_T3_A05_D21_14
- U2301 pad 10: B34_L15_N -> IO_L8N_T1_AD10N_15
- U2301 pad 11: B34_L15_P -> IO_L9N_T1_DQS_AD3N_15
- U2301 pad 12: B34_L18_N -> IO_L10N_T1_AD11N_15
- U2301 pad 13: B34_L2_P -> IO_L13N_T2_MRCC_15
- U2301 pad 14: B34_L2_N -> IO_L15P_T2_DQS_15
- U2301 pad 15: B34_L12_P -> IO_L15N_T2_DQS_ADV_B_15
- U2301 pad 17: B34_L6_N -> IO_L16P_T2_A28_15
- U2301 pad 18: B34_L6_P -> IO_L16N_T2_A27_15
- U2301 pad 19: B34_L8_P -> IO_L18P_T2_A24_15
- U2301 pad 20: B35_L16_P -> IO_L18N_T2_A23_15
- U2301 pad 21: B35_L16_N -> IO_L14N_T2_SRCC_15
- U2301 pad 22: B34_L7_N -> IO_L13P_T2_MRCC_15
- U2301 pad 23: B35_L18_N -> IO_L17N_T2_A25_15
- U2301 pad 24: B35_L18_P -> IO_L17P_T2_A26_15
- U2301 pad 25: B35_L21_P -> IO_L24N_T3_RS0_15
- U2301 pad 26: B35_L15_N -> IO_L14P_T2_SRCC_15
- U2301 pad 28: B35_L15_P -> IO_L19N_T3_A21_VREF_15
- U2301 pad 29: B35_L8_P -> IO_L24P_T3_RS1_15
- U2301 pad 30: B35_L13_P -> IO_L19P_T3_A22_15
- U2301 pad 32: B35_L13_N -> IO_L23N_T3_FWE_B_15
- U2301 pad 33: B35_L11_N -> IO_L20N_T3_A19_15
- U2301 pad 34: B35_L14_P -> IO_L2N_T0_D03_14
- U2301 pad 35: B35_L14_N -> IO_L23P_T3_FOE_B_15
- U2301 pad 36: B35_L3_N -> IO_L3N_T0_DQS_EMCCLK_14
- U2301 pad 37: B35_L12_P -> IO_L8P_T1_D11_14
- U2301 pad 38: B35_L12_N -> IO_L4P_T0_D04_14
- U2301 pad 40: B35_L7_N -> IO_L4N_T0_D05_14
- U2301 pad 41: B35_L23_N -> IO_L7P_T1_D09_14
- U2301 pad 42: B35_L23_P -> IO_L7N_T1_D10_14
- U2301 pad 43: B35_L4_P -> IO_L10P_T1_D14_14
- U2301 pad 44: B35_L2_N -> IO_L6N_T0_D08_VREF_14
- U2301 pad 45: B35_L2_P -> IO_L9P_T1_DQS_14
- U2301 pad 46: B35_L5_N -> IO_L8N_T1_D12_14
- U2301 pad 47: B35_L17_P -> IO_L10N_T1_D15_14
- U2301 pad 48: B35_L17_N -> IO_L11P_T1_SRCC_14
- U2301 pad 49: B35_L6_N -> IO_L9N_T1_DQS_D13_14
- U2301 pad 52: B35_L24_P -> IO_L15P_T2_DQS_RDWR_B_14
- U2301 pad 53: B35_L24_N -> IO_L12N_T1_MRCC_14
- U2301 pad 57: B35_L0 -> IO_L11N_T1_SRCC_14
- U2301 pad 62: B35_L9_N -> IO_L14P_T2_SRCC_14
- U2301 pad 63: B35_L9_P -> IO_L15N_T2_DQS_DOUT_CSO_B_14
- U2301 pad 64: B35_L22_N -> IO_L14N_T2_SRCC_14
- U2301 pad 65: B35_L22_P -> IO_L16P_T2_CSI_B_14
- U2301 pad 66: B35_L10_N -> IO_L16N_T2_A15_D31_14
- U3 pad 1: FIFO_D1 -> IO_L12N_T1_MRCC_34
- U3 pad 17: FIFO_TXF -> IO_L16N_T2_34
- U3 pad 18: FIFO_RXE -> IO_L15P_T2_DQS_34
- U3 pad 19: FIFO_CLK -> IO_L12P_T1_MRCC_34
- U3 pad 2: FIFO_D7 -> IO_L11P_T1_SRCC_34
- U3 pad 20: USB_PWRENb -> IO_L15N_T2_DQS_34
- U3 pad 21: FIFO_D0 -> IO_L14N_T2_SRCC_34
- U3 pad 22: FIFO_D4 -> IO_L14P_T2_SRCC_34
- U3 pad 23: FIFO_D2 -> IO_L13N_T2_MRCC_34
- U3 pad 4: FIFO_D5 -> IO_L13P_T2_MRCC_34
- U3 pad 5: FIFO_D6 -> IO_L9N_T1_DQS_34
- U3 pad 6: FIFO_D3 -> IO_L11N_T1_SRCC_34
- U3 pad 7: FIFO_SIWU -> IO_L9P_T1_DQS_34
- U3 pad 8: FIFO_RDb -> IO_L7P_T1_34
- U3 pad 9: FIFO_WRb -> IO_L7N_T1_34
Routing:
- net B35_L3_N: track 61.6 -> 0.00 mm, vias 2 -> 0
- net IO_L3N_T0_DQS_EMCCLK_14: track 1.60 -> 63.2 mm, vias 0 -> 2
- net B35_L25: track 47.1 -> 0.00 mm
- net /lan9254/LINKACT0: track 112.3 -> 66.4 mm, vias 5 -> 2
- net B35_L20_P: track 40.8 -> 0.00 mm
- net B35_L9_N: track 38.4 -> 0.00 mm
- net IO_L16N_T2_A15_D31_14: track 3.29 -> 40.0 mm
- net B35_L10_N: track 36.7 -> 0.00 mm
- net IO_L16P_T2_CSI_B_14: track 3.09 -> 38.5 mm
- net B35_L22_P: track 35.4 -> 0.00 mm
- net IO_L14N_T2_SRCC_14: track 2.99 -> 37.0 mm
- net B35_L22_N: track 34.0 -> 0.00 mm
- net IO_L15N_T2_DQS_DOUT_CSO_B_14: track 1.50 -> 34.1 mm
- net B35_L9_P: track 32.6 -> 0.00 mm
- net IO_L14P_T2_SRCC_14: track 3.21 -> 34.8 mm
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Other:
- net class Default: clearance 0.0889 -> 0.1
- net class diffp: clearance 0.0889 -> 0.1; trace_width 0.0889 -> 0.1
- net class diffp_ec: clearance 0.0889 -> 0.1; trace_width 0.0889 -> 0.1
- rule trace_clearance: 0.0889 -> 0.1
- rule trace_min: 0.0889 -> 0.09

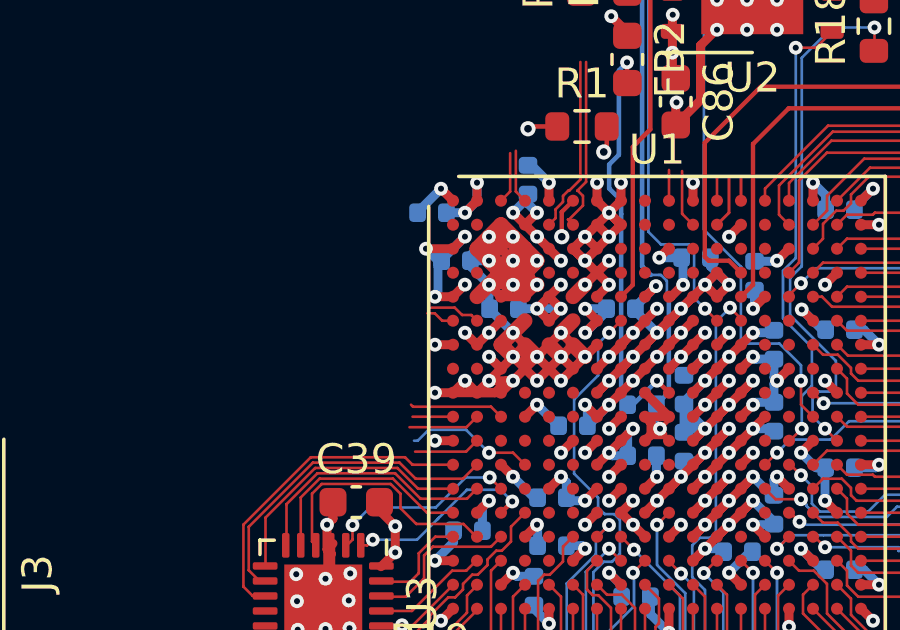
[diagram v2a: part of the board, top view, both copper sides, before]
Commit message: PCB: reverted design rules to JLCPCB process; starting point before relaxing!
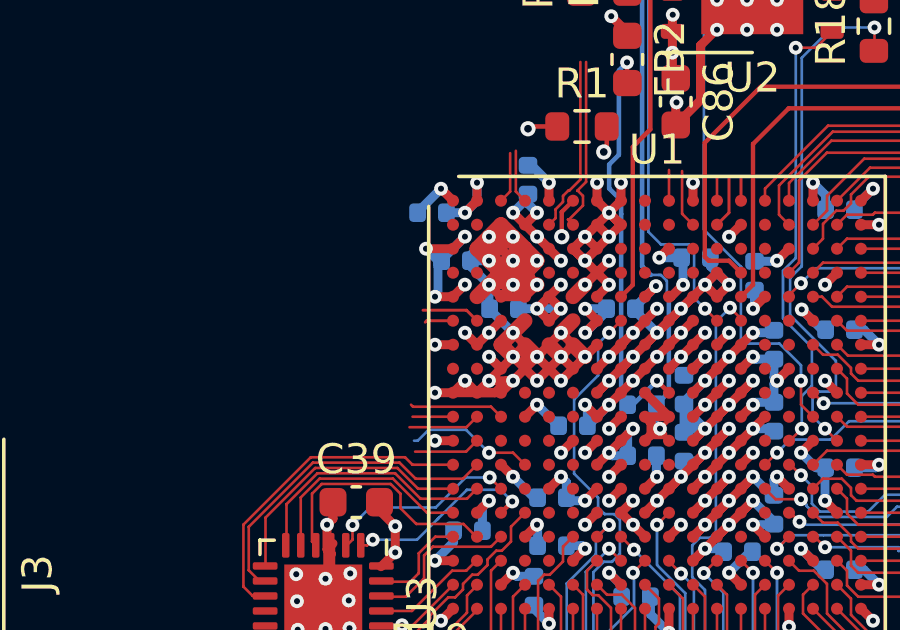
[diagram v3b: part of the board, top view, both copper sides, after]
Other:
- net class Default: clearance 0.1 -> 0.0889; trace_width 0.1524 -> 0.0889
- rule trace_clearance: 0.1 -> 0.0889
- rule trace_min: 0.09 -> 0.0889
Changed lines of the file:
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@@
     (thickness 1.6)
     (drawings 5)
-    (tracks 3441)
+    (tracks 3438)
     (zones 0)
     (modules 359)
@@
   )
   (setup
-    (last_trace_width 0.5)
+    (last_trace_width 0.0889)
+    (user_trace_width 0.0889)
     (user_trace_width 0.1)
     (user_trace_width 0.147)
@@
     (user_trace_width 1)
     (user_trace_width 2.54)
-    (trace_clearance 0.1)
+    (trace_clearance 0.0889)
     (zone_clearance 0.1524)
     (zone_45_only no)
-    (trace_min 0.09)
+    (trace_min 0.0889)
     (via_size 0.508)
     (via_drill 0.254)
@@
   (net 360 "Net-(R87-Pad1)")
   (net_class Default "This is the default net class."
-    (clearance 0.1)
-    (trace_width 0.1524)
+    (clearance 0.0889)
+    (trace_width 0.0889)
     (via_dia 0.508)
     (via_drill 0.254)
@@
     (uvia_drill 0.1)
     (diff_pair_width 0.1)
-    (diff_pair_gap 0.1016)
+    (diff_pair_gap 0.0889)
     (add_net /lan9254/rj45_ports/P0_RXD_N)
     (add_net /lan9254/rj45_ports/P0_RXD_P)
@@
   (segment (start 134.695249 35.89525) (end 134.999999 36.2) (width 0.0889) (layer F.Cu) (net 8))
   (segment (start 134.139454 35.89525) (end 134.695249 35.89525) (width 0.0889) (layer F.Cu) (net 8))
-  (segment (start 46.256711 76.763351) (end 45.425591 76.763351) (width 0.0889) (layer F.Cu) (net 8))
-  (segment (start 46.50286 77.0095) (end 46.256711 76.763351) (width 0.0889) (layer F.Cu) (net 8))
-  (segment (start 46.8095 77.0095) (end 46.50286 77.0095) (width 0.0889) (layer F.Cu) (net 8))
-  (segment (start 47 77.2) (end 46.8095 77.0095) (width 0.0889) (layer F.Cu) (net 8))
+  (segment (start 46.649999 76.849999) (end 45.200001 76.849999) (width 0.1) (layer F.Cu) (net 8))
+  (segment (start 47 77.2) (end 46.649999 76.849999) (width 0.1) (layer F.Cu) (net 8))
   (segment (start 134.695249 35.70475) (end 134.999999 35.4) (width 0.0889) (layer F.Cu) (net 9))
   (segment (start 134.999999 35.4) (end 136.5 35.4) (width 0.0889) (layer F.Cu) (net 9) (status 20))
   (segment (start 134.060546 35.70475) (end 134.695249 35.70475) (width 0.0889) (layer F.Cu) (net 9))
-  (segment (start 45.840296 77.2) (end 45.594138 76.953842) (width 0.0889) (layer F.Cu) (net 9))
-  (segment (start 46.2 77.2) (end 45.840296 77.2) (width 0.0889) (layer F.Cu) (net 9))
-  (segment (start 45.594138 76.953842) (end 45.346688 76.953842) (width 0.0889) (layer F.Cu) (net 9))
+  (segment (start 46.2 77.2) (end 45.325 77.2) (width 0.1) (layer F.Cu) (net 9))
+  (segment (start 45.325 77.2) (end 45.275 77.25) (width 0.1) (layer F.Cu) (net 9))
   (segment (start 52.6 85.2) (end 52.6 85.133838) (width 0.0889) (layer F.Cu) (net 14))
   (via (at 52.2 85.6) (size 0.46) (drill 0.2) (layers F.Cu B.Cu) (net 14))
